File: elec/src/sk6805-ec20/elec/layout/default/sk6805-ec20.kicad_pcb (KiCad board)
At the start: 2 copper layers, 225.7 x 100.8 mm, 2 parts

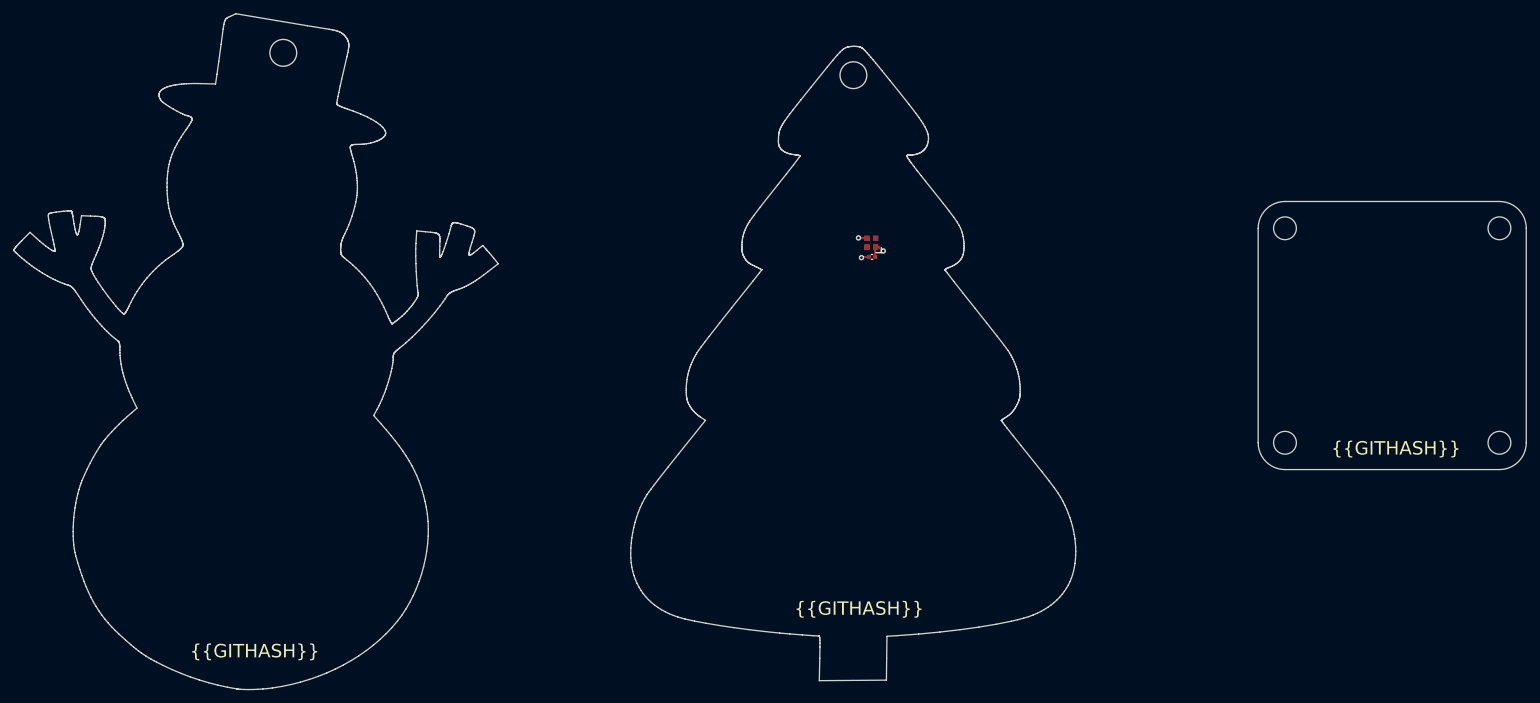
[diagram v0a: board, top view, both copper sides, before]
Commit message: Add layout for base
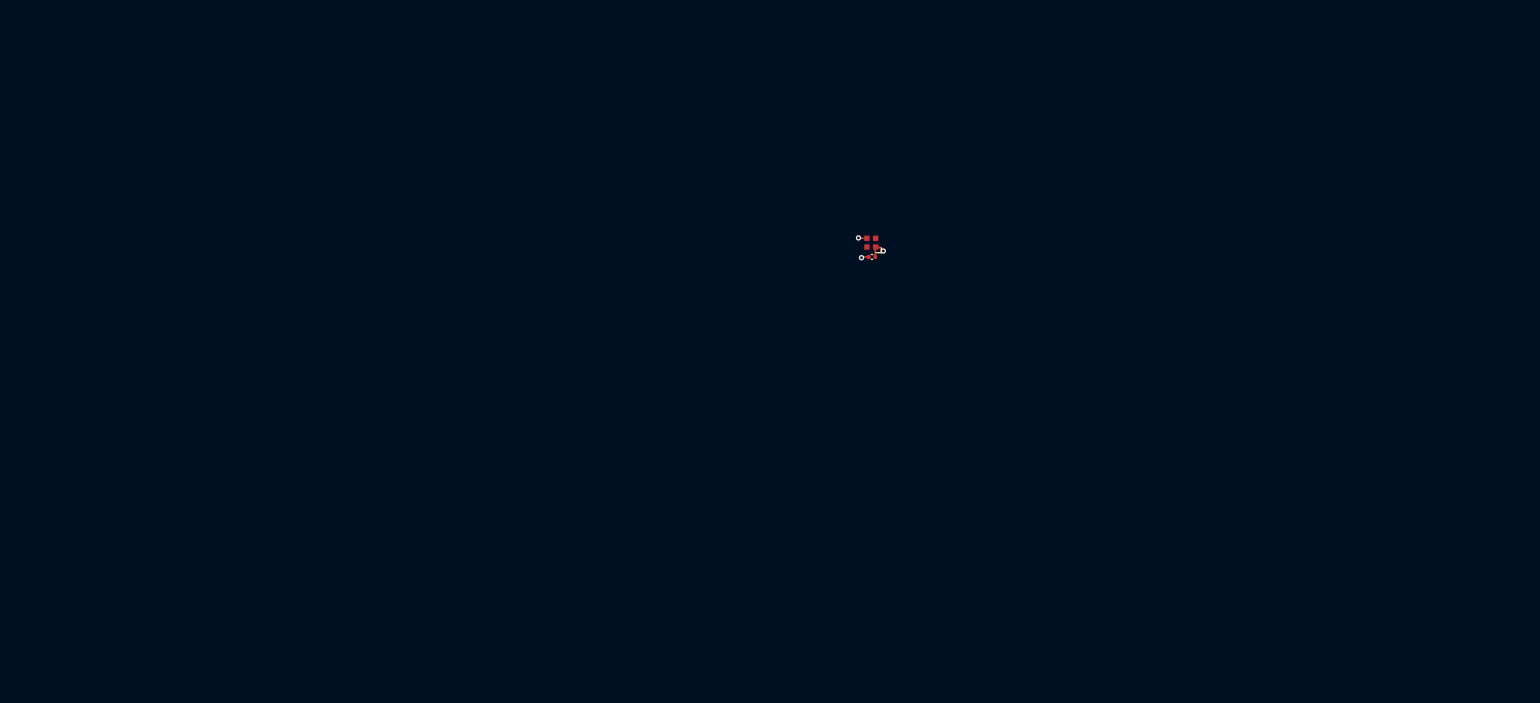
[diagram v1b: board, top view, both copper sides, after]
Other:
- board outline removed
- board text removed: "{{GITHASH}}"
